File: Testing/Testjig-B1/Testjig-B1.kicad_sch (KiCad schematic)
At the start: 1 part, among them X1 5102159-8

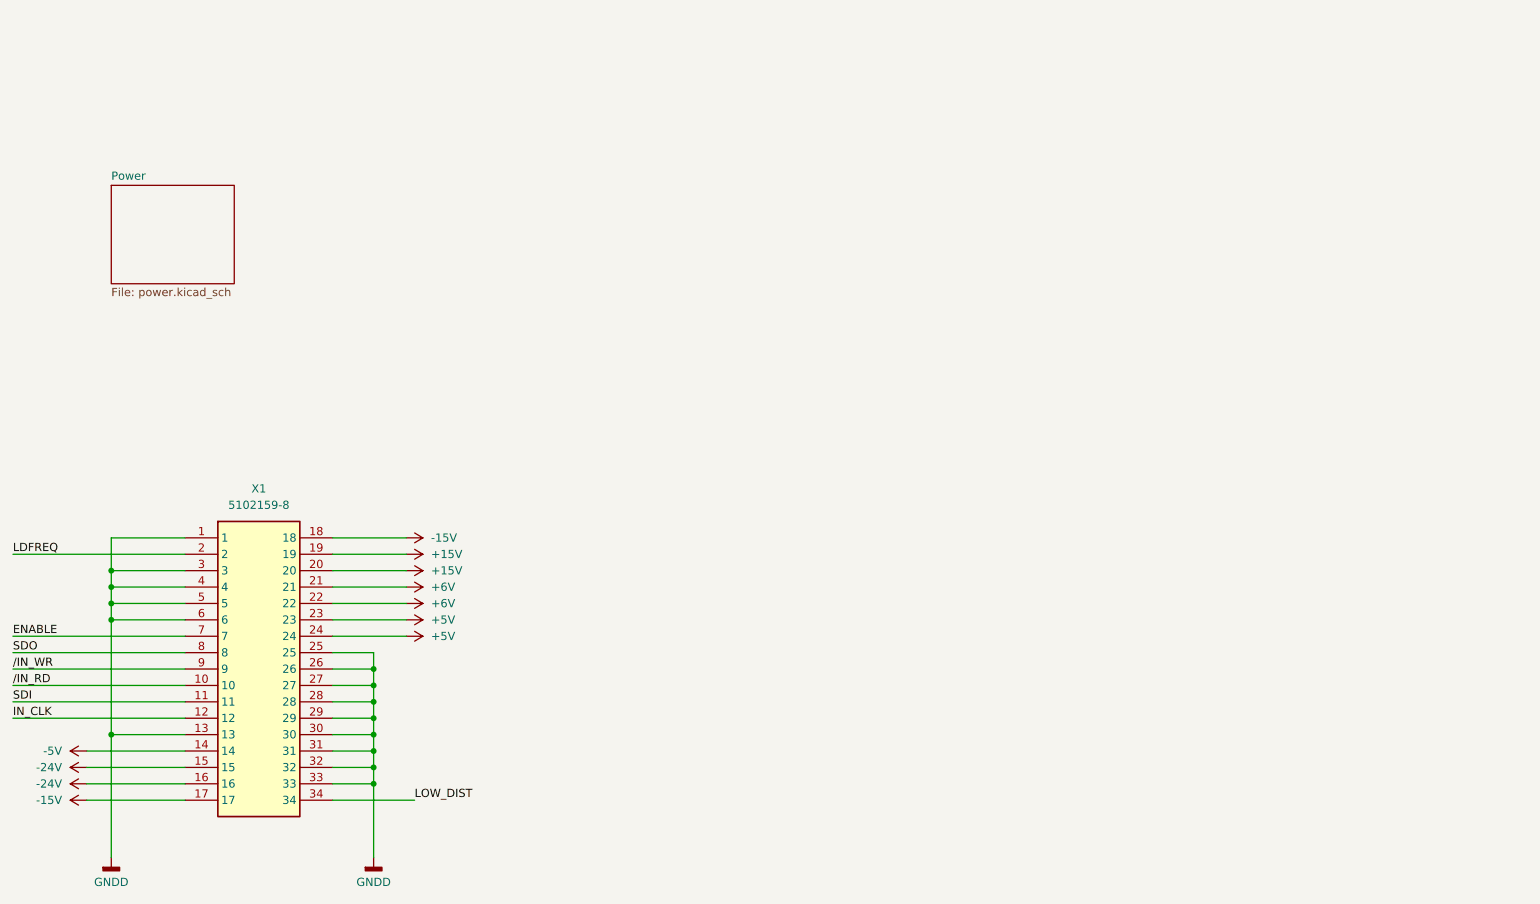
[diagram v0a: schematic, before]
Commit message: Add CPU and level shifter
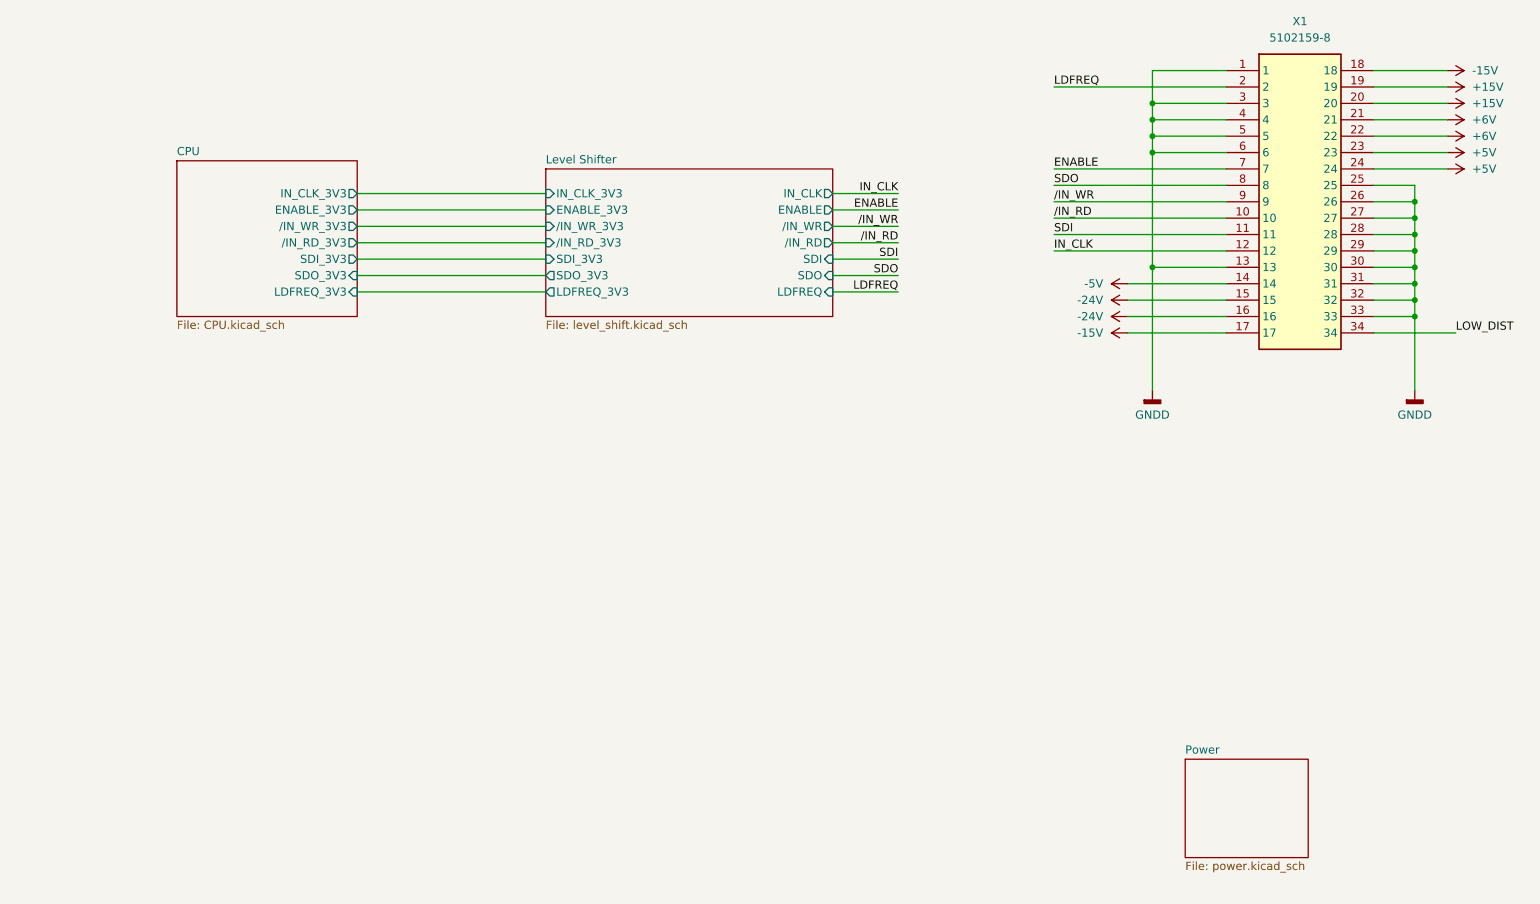
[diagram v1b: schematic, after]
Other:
- added sheet CPU (CPU.kicad_sch)
- added sheet Level Shifter (level_shift.kicad_sch)
- moved on the sheet: X1

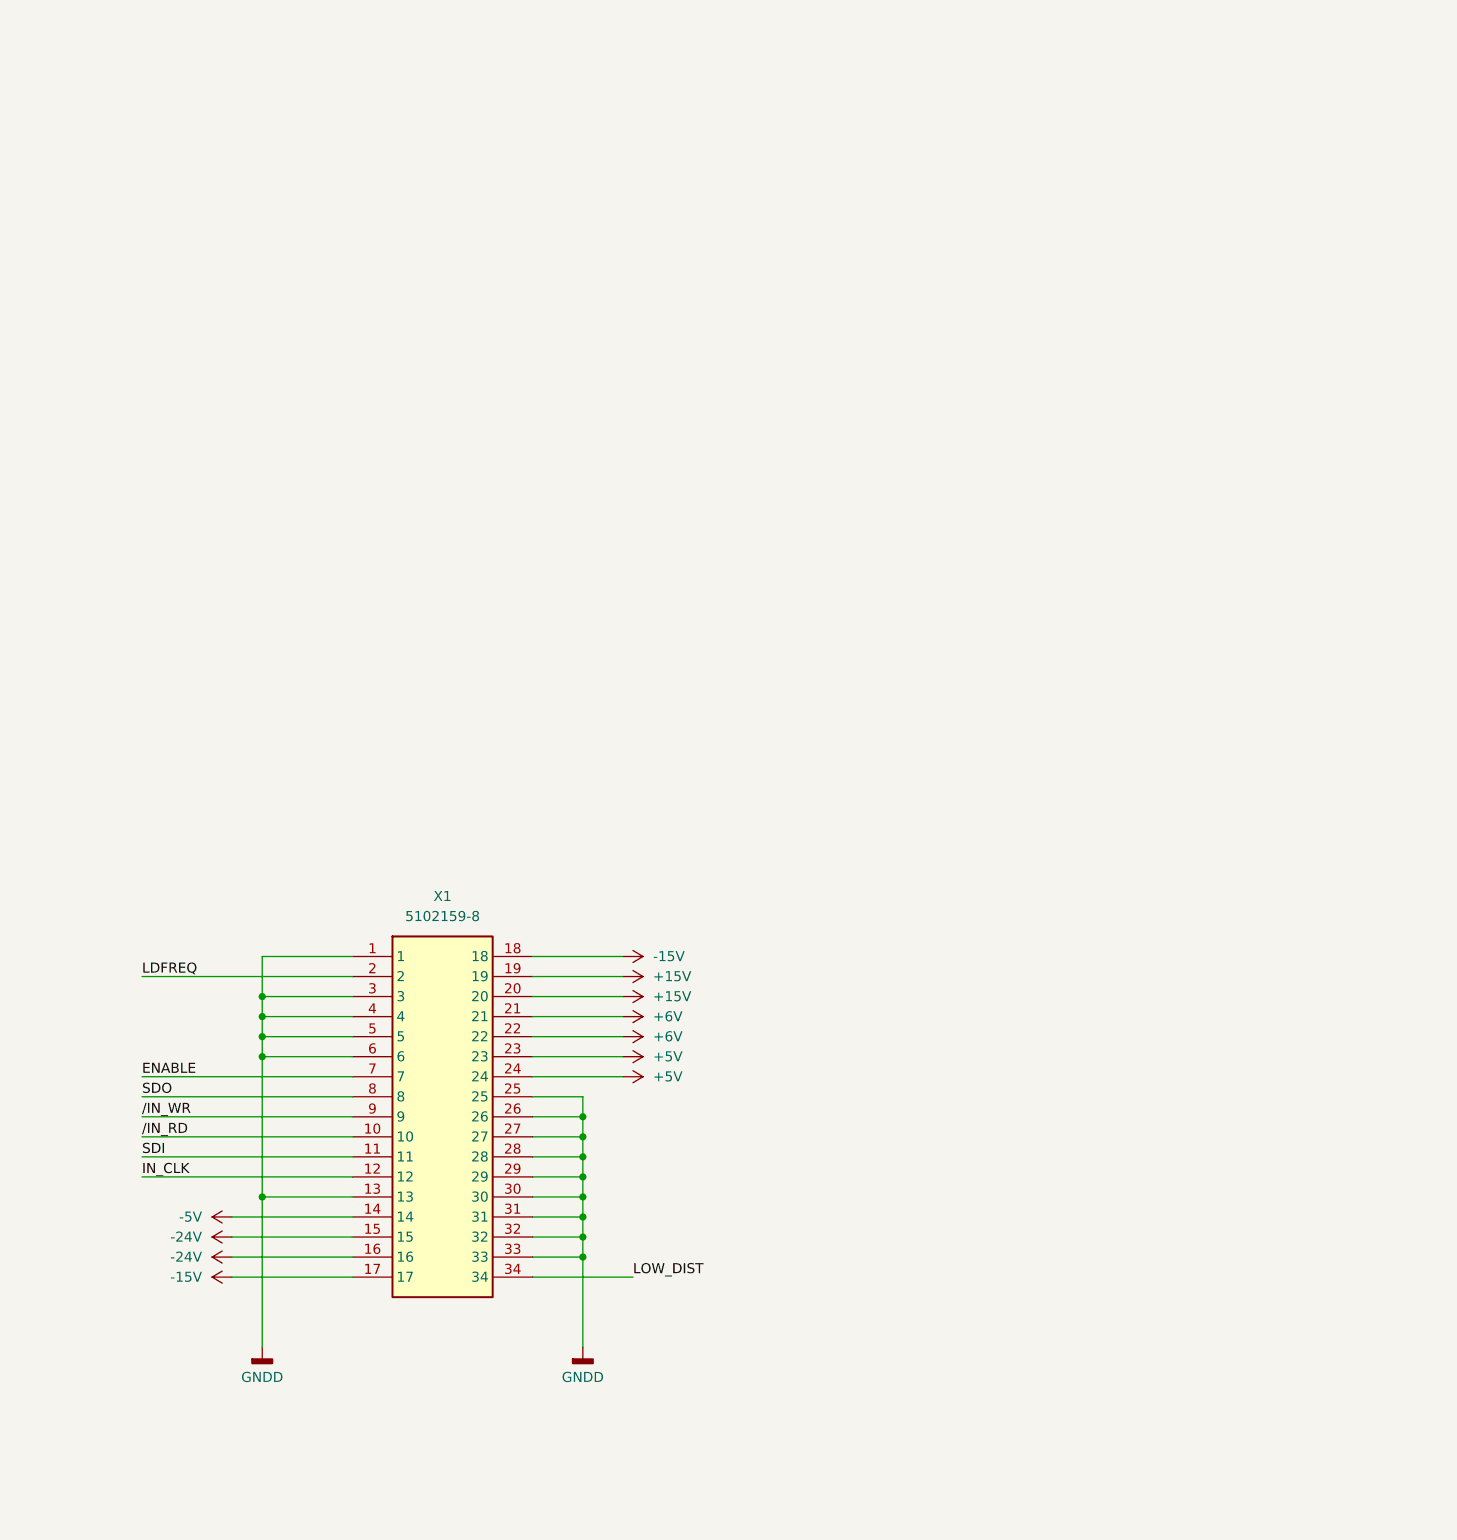
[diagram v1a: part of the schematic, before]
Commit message: Rework connector to be alternating left/right.
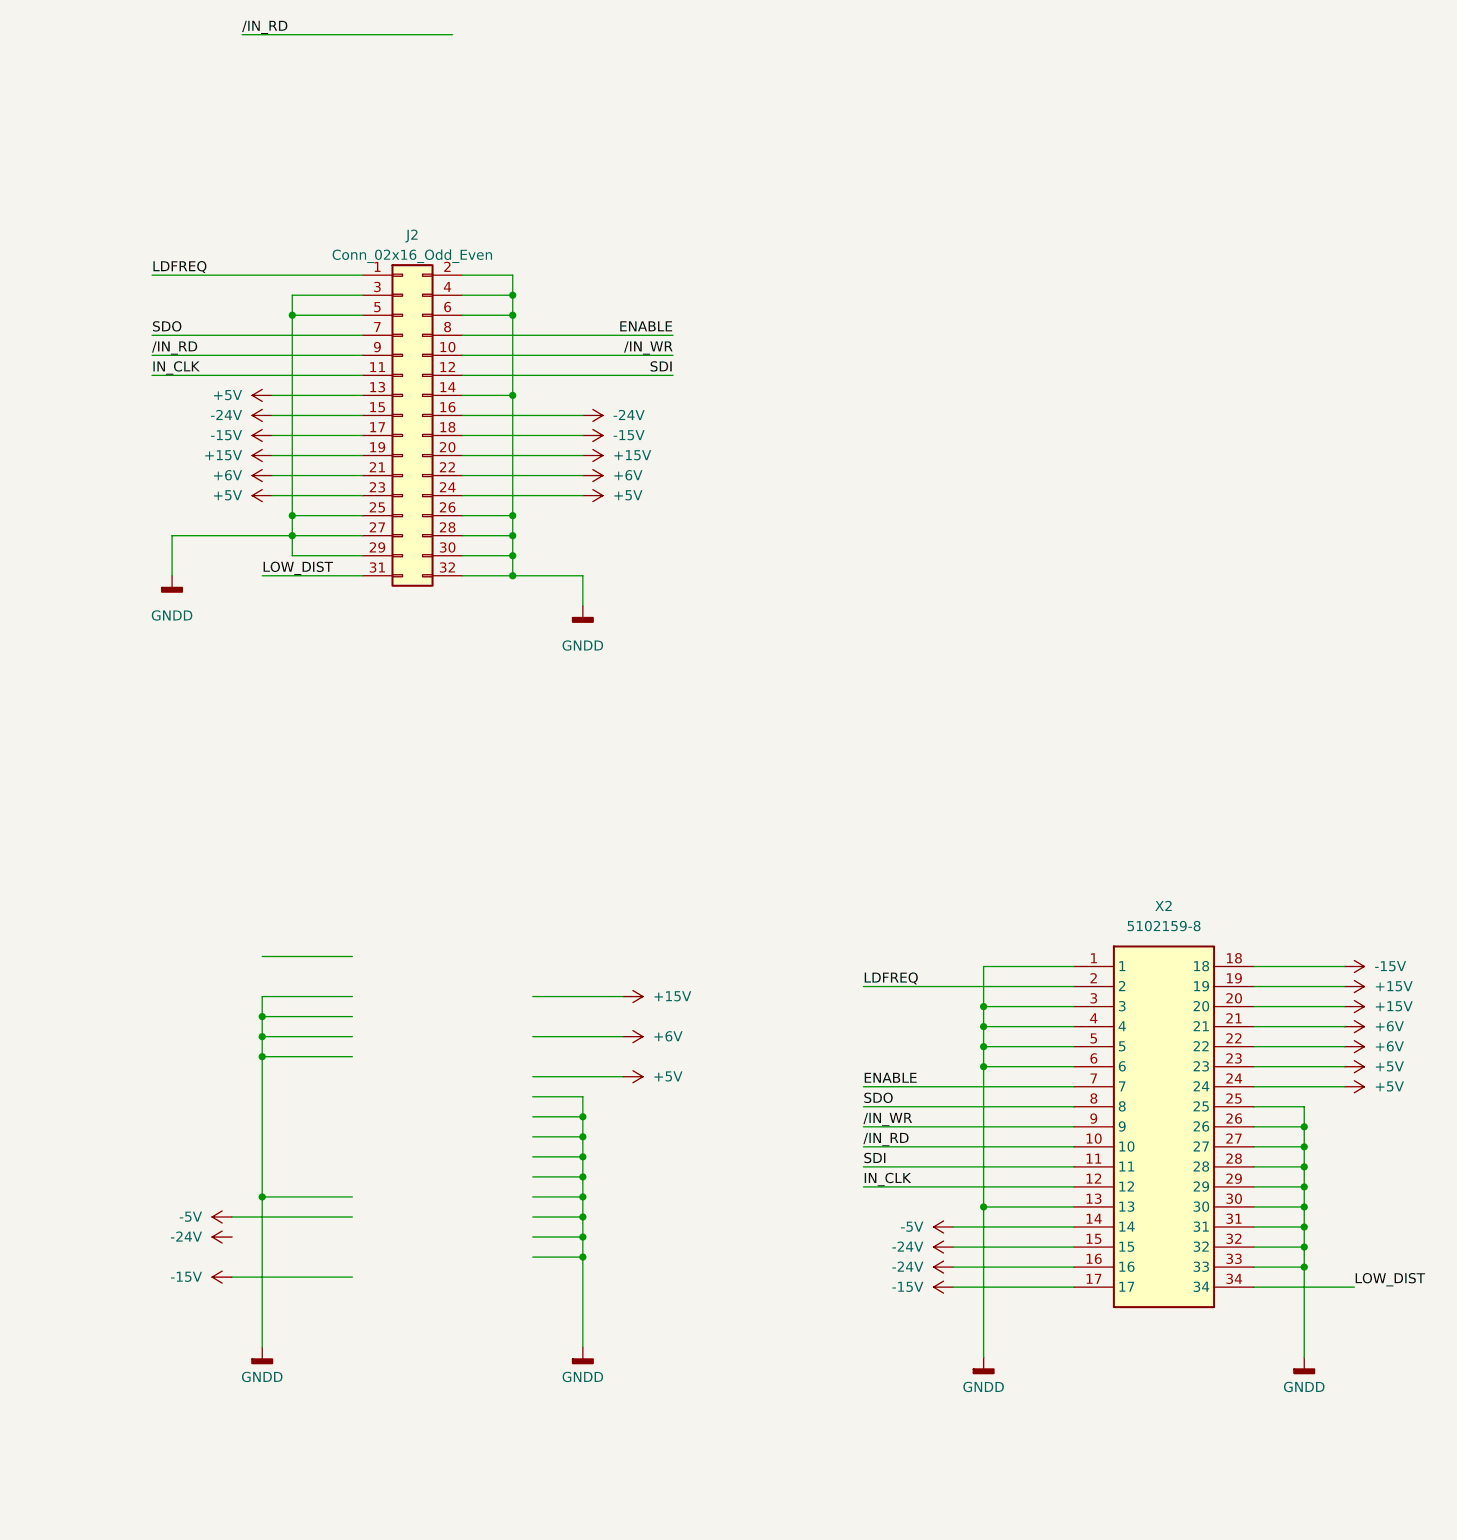
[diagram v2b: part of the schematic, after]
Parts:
- removed X1: 5102159-8, UPL_B1:CONN_5103311-7_TYC, symbol UPL_B1:5102159-8
- added J2: Conn_02x16_Odd_Even, symbol Connector_Generic:Conn_02x16_Odd_Even
- added X2: 5102159-8, UPL_B1:CONN_5103311-7_TYC, symbol UPL_B1:5102159-8
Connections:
- net +15V: now also J2.19 (Pin_19), J2.20 (Pin_20), X2.19, X2.20
- net +5V: now also J2.13 (Pin_13), J2.23 (Pin_23), J2.24 (Pin_24), X2.23, X2.24
- net +6V: now also J2.21 (Pin_21), J2.22 (Pin_22), X2.21, X2.22
- net -15V: now also J2.17 (Pin_17), J2.18 (Pin_18), X2.17, X2.18
- net -24V: now also J2.15 (Pin_15), J2.16 (Pin_16), X2.15, X2.16
- net -5V: now also X2.14
- net ENABLE: now also J2.8 (Pin_8), X2.7
- net GNDD: now also J2.14 (Pin_14), J2.2 (Pin_2), J2.25 (Pin_25), J2.26 (Pin_26), J2.27 (Pin_27), J2.28 (Pin_28), J2.29 (Pin_29), J2.3 (Pin_3), J2.30 (Pin_30), J2.32 (Pin_32), J2.4 (Pin_4), J2.5 (Pin_5), J2.6 (Pin_6), X2.1, X2.13, X2.25, X2.26, X2.27, X2.28, X2.29, X2.3, X2.30, X2.31, X2.32, X2.33, X2.4, X2.5, X2.6
- net IN_CLK: now also J2.11 (Pin_11), X2.12
- net LDFREQ: now also J2.1 (Pin_1), X2.2
- net LOW_DIST: now also J2.31 (Pin_31), X2.34
- net SDI: now also J2.12 (Pin_12), X2.11
- net SDO: now also J2.7 (Pin_7), X2.8
- net /IN_RD: now also J2.9 (Pin_9), X2.10
- net /IN_WR: now also J2.10 (Pin_10), X2.9
